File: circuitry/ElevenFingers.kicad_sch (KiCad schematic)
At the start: 95 parts, among them J1 OLED, SW1 MX, SW10 MX, SW11 MX, SW12 MX, SW13 MX, SW14 MX, SW15 MX, SW16 MX, SW17 MX, SW18 MX, SW19 MX, SW2 MX, SW20 MX, SW21 MX, SW22 MX, SW23 MX, SW24 MX, SW25 MX, SW26 MX, SW27 MX, SW28 MX, SW29 MX, SW3 MX, SW30 MX, SW4 MX, SW5 MX, SW6 MX, SW7 MX, SW8 MX, SW9 MX, U1 ProMicro, U2 TRRS

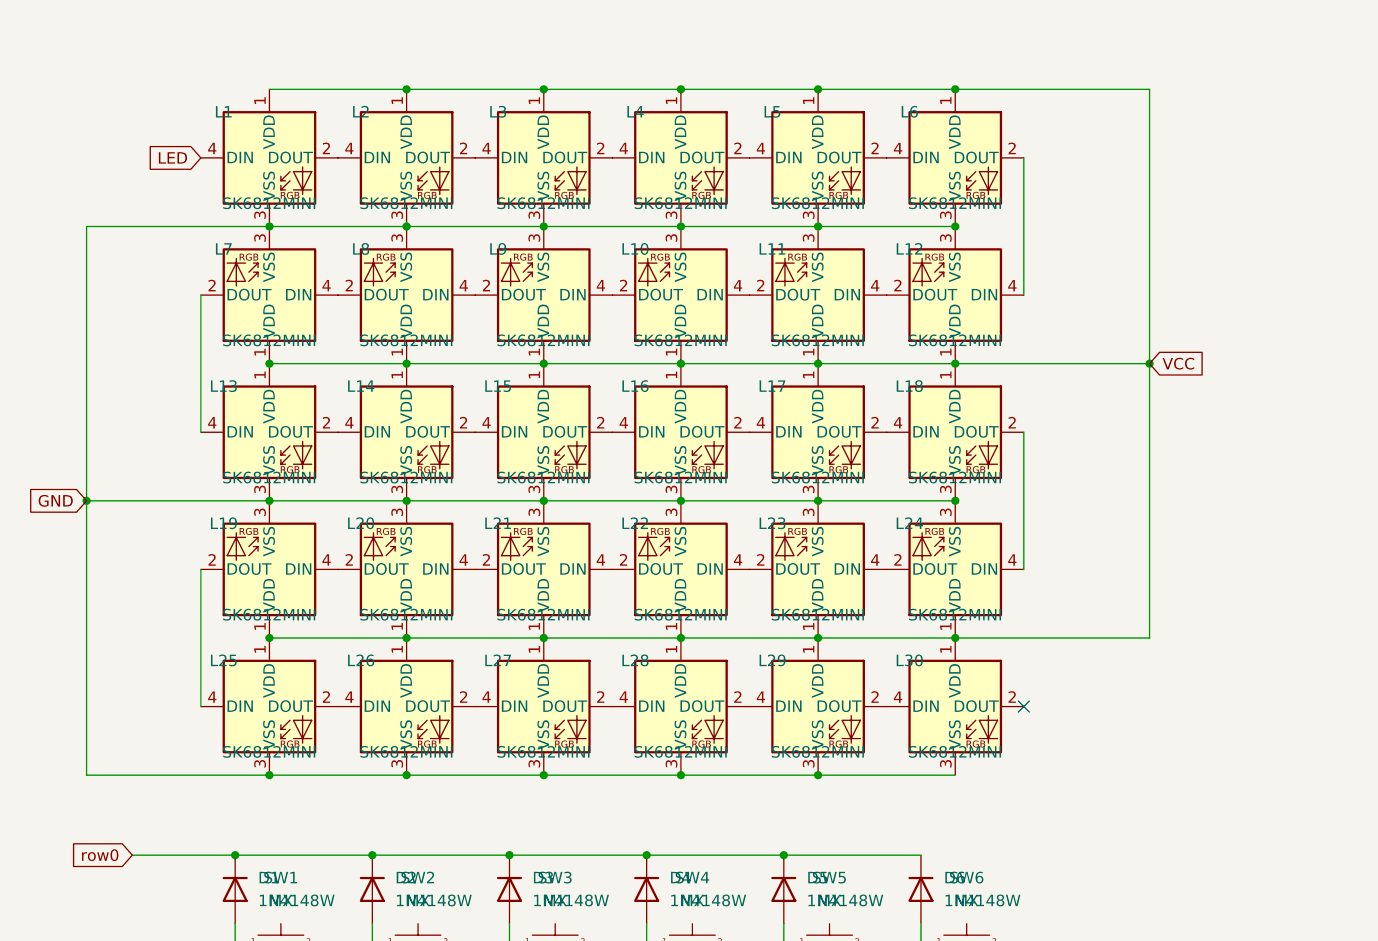
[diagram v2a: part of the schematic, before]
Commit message: all components traced internally, not yet connected
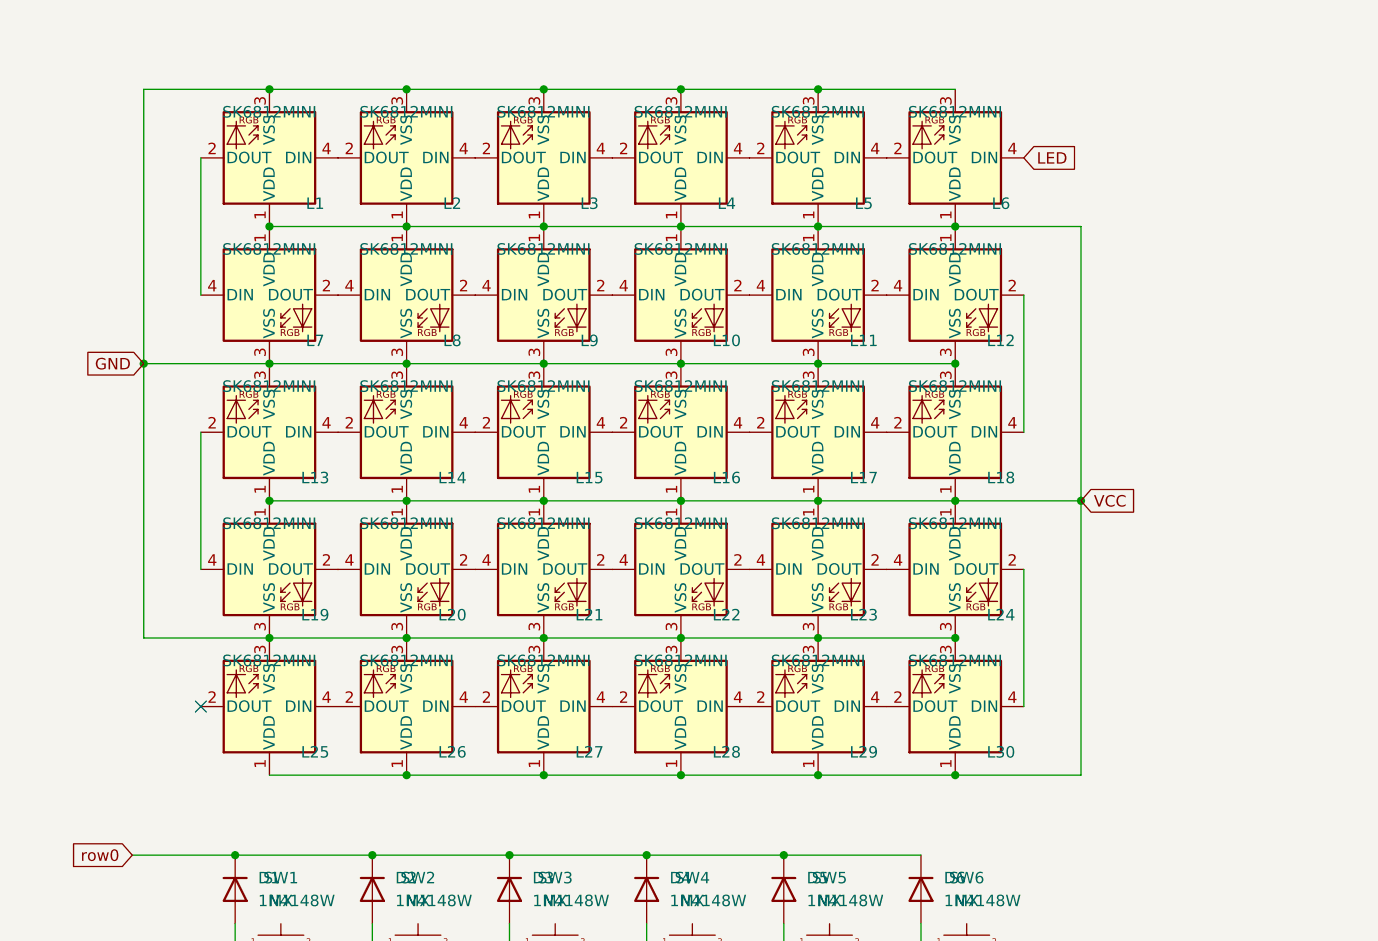
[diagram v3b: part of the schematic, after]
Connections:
- net LED: now also L6.4 (DIN); no longer L1.4 (DIN)
- net at L17.2 (DOUT): now also L16.4 (DIN); no longer L18.4 (DIN)
- net at L17.4 (DIN): now also L18.2 (DOUT); no longer L16.2 (DOUT)
- net at L4.2 (DOUT): now also L3.4 (DIN); no longer L5.4 (DIN)
- net at L4.4 (DIN): now also L5.2 (DOUT); no longer L3.2 (DOUT)
- net at L24.4 (DIN): now also L23.2 (DOUT); no longer L18.2 (DOUT)
- net at L2.2 (DOUT): now also L1.4 (DIN); no longer L3.4 (DIN)
- net at L2.4 (DIN): now also L3.2 (DOUT); no longer L1.2 (DOUT)
- net at L22.4 (DIN): now also L21.2 (DOUT); no longer L23.2 (DOUT)
- net at L23.4 (DIN): now also L22.2 (DOUT); no longer L24.2 (DOUT)
- net at L20.4 (DIN): now also L19.2 (DOUT); no longer L21.2 (DOUT)
- net at L21.4 (DIN): now also L20.2 (DOUT); no longer L22.2 (DOUT)
- net at L14.2 (DOUT): now also L13.4 (DIN); no longer L15.4 (DIN)
- net at L14.4 (DIN): now also L15.2 (DOUT); no longer L13.2 (DOUT)
- net at L26.2 (DOUT): now also L25.4 (DIN); no longer L27.4 (DIN)
- net at L26.4 (DIN): now also L27.2 (DOUT); no longer L25.2 (DOUT)
- net at L29.2 (DOUT): now also L28.4 (DIN); no longer L30.4 (DIN)
- net at L29.4 (DIN): now also L30.2 (DOUT); no longer L28.2 (DOUT)
- net at L10.2 (DOUT): now also L11.4 (DIN); no longer L9.4 (DIN)
- net at L10.4 (DIN): now also L9.2 (DOUT); no longer L11.2 (DOUT)
- net at L12.2 (DOUT): now also L18.4 (DIN); no longer L11.4 (DIN)
- net at L12.4 (DIN): now also L11.2 (DOUT); no longer L6.2 (DOUT)
- net at L8.4 (DIN): now also L7.2 (DOUT); no longer L9.2 (DOUT)
- net at L19.4 (DIN): now also L13.2 (DOUT); no longer L20.2 (DOUT)
- net at L8.2 (DOUT): now also L9.4 (DIN); no longer L7.4 (DIN)
- new net: L24.2 (DOUT), L30.4 (DIN)
- new net: L15.4 (DIN), L16.2 (DOUT)
- new net: L27.4 (DIN), L28.2 (DOUT)
- new net: L1.2 (DOUT), L7.4 (DIN)
- new net: L5.4 (DIN), L6.2 (DOUT)
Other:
- moved on the sheet: L1, L10, L11, L12, L13, L14, L15, L16, L17, L18, L19, L2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
